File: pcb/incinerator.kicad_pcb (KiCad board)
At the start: 2 copper layers, 51 parts, among them J1 Power Source 12V, J2 IGNITION_MAIN, J3 IGNITION_AFT, J4 VALVE_MAIN, J5 VALVE_AFT_HI, J6 VALVE_AFT_LO, J7 AIRPMP, J8 To Rotary Encoder / Switch, J9 Waveshare 4.2" e-paper, Q1 IRLU120N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

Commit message: First draft of PCB layout
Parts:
- D10: value GRN -> RED
- D11, D9: value GRN -> D; footprint LED_THT:LED_D3.0mm -> Diode_THT:D_DO-41_SOD81_P10.16mm_Horizontal
- D12: value YLW -> RED
- D3, D5: value D -> RED; footprint Diode_THT:D_DO-41_SOD81_P10.16mm_Horizontal -> LED_THT:LED_D3.0mm
- R11, R8: value 15k -> 100
- R12, R9: value 15k -> 1k
- R14, R17: value 100 -> 15k
- R16: value 100 -> 1k
- R3, R6: value 1k -> 15k
- R4: value 1k -> 100
- moved U3 186.9 mm to (91.4, 22.9)
- moved D1 144.8 mm to (38.1, 20.3), turned to 270 degrees
- moved U4 139.9 mm to (129.5, 22.9)
- moved C1 138.2 mm to (40.6, 129.5), turned to 270 degrees
- moved J9 127.9 mm to (154.9, 104.1)
- moved J8 119.5 mm to (109.2, 73.7), turned to 180 degrees
- moved D9 112.1 mm to (38.1, 91.4), turned to 270 degrees
- moved D8 102.4 mm to (58.4, 76.2), turned to 90 degrees
- moved R7 102.1 mm to (48.3, 33.0)
- moved R12 100.4 mm to (53.3, 91.4), turned to 180 degrees
- moved R13 99.7 mm to (61.0, 27.9)
- moved BZ1 97.9 mm to (129.5, 63.5), turned to 180 degrees
- moved D2 94.9 mm to (38.1, 38.1), turned to 270 degrees
- moved R4 94.4 mm to (61.0, 45.7)
- moved D10 94.4 mm to (58.4, 94.0), turned to 90 degrees
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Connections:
- D11 pad 1: Net-(D11-Pad1) -> +12V
- D12 pad 1: Net-(D12-Pad1) -> Net-(D11-Pad2)
- D3 pad 1: +12V -> Net-(D2-Pad2)
- D4 pad 2: Net-(D10-Pad1) -> Net-(D4-Pad2)
- D5 pad 1: +12V -> Net-(D4-Pad2)
- D5 pad 2: Net-(D11-Pad1) -> Net-(D5-Pad2)
- D6 pad 2: Net-(D12-Pad1) -> Net-(D6-Pad2)
- D8 pad 1: Net-(D2-Pad2) -> Net-(D6-Pad2)
- D9 pad 1: Net-(D3-Pad2) -> +12V
- D9 pad 2: Net-(D9-Pad2) -> Net-(D10-Pad1)
- J4 pad 2: Net-(D3-Pad2) -> Net-(D4-Pad2)
- J5 pad 2: Net-(D10-Pad1) -> Net-(D6-Pad2)
- J6 pad 2: Net-(D11-Pad1) -> Net-(D10-Pad1)
- J7 pad 2: Net-(D12-Pad1) -> Net-(D11-Pad2)
- Q3 pad 2: Net-(D3-Pad2) -> Net-(D4-Pad2)
- Q4 pad 2: Net-(D10-Pad1) -> Net-(D6-Pad2)
- Q5 pad 2: Net-(D11-Pad1) -> Net-(D10-Pad1)
- Q6 pad 2: Net-(D12-Pad1) -> Net-(D11-Pad2)
- R11 pad 1: Earth -> Net-(Q4-Pad1)
- R11 pad 2: Net-(Q5-Pad1) -> Net-(R11-Pad2)
- R12 pad 1: Earth -> Net-(D10-Pad2)
- R12 pad 2: Net-(Q6-Pad1) -> +12V
- R14 pad 1: Net-(Q2-Pad1) -> Earth
- R14 pad 2: Net-(R14-Pad2) -> Net-(Q5-Pad1)
- R15 pad 1: Net-(Q3-Pad1) -> Net-(Q5-Pad1)
- R16 pad 1: Net-(Q4-Pad1) -> Net-(D12-Pad2)
- R16 pad 2: Net-(R16-Pad2) -> +12V
- R17 pad 1: Net-(Q5-Pad1) -> Earth
- R17 pad 2: Net-(R17-Pad2) -> Net-(Q6-Pad1)
- R2 pad 1: Net-(D8-Pad2) -> Net-(D3-Pad2)
- R3 pad 1: Net-(D9-Pad2) -> Earth
- R3 pad 2: +12V -> Net-(Q2-Pad1)
- R4 pad 1: Net-(D10-Pad2) -> Net-(Q2-Pad1)
- R4 pad 2: +12V -> Net-(R4-Pad2)
- R5 pad 1: Net-(D11-Pad2) -> Net-(D5-Pad2)
- R6 pad 1: Net-(D12-Pad2) -> Earth
- R6 pad 2: +12V -> Net-(Q3-Pad1)
- R8 pad 1: Earth -> Net-(Q3-Pad1)
- R8 pad 2: Net-(Q2-Pad1) -> Net-(R8-Pad2)
- R9 pad 1: Earth -> Net-(D8-Pad2)
- R9 pad 2: Net-(Q3-Pad1) -> +12V
- U2 pad 10: Net-(R17-Pad2) -> Net-(R15-Pad2)
- U2 pad 7: Net-(R14-Pad2) -> Net-(R4-Pad2)
- U2 pad 8: Net-(R15-Pad2) -> Net-(R8-Pad2)
- U2 pad 9: Net-(R16-Pad2) -> Net-(R11-Pad2)
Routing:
- net Earth: track 0.00 -> 520.4 mm, vias 0 -> 18
- net +12V: track 0.00 -> 259.1 mm, vias 0 -> 7
- net +3V3: track 0.00 -> 177.8 mm, vias 0 -> 2
- net /CLK: track 0.00 -> 152.4 mm, vias 0 -> 4
- net Net-(U2-Pad21): track 0.00 -> 139.7 mm, vias 0 -> 4
- net Net-(U2-Pad25): track 0.00 -> 109.2 mm, vias 0 -> 2
- net Net-(U2-Pad20): track 0.00 -> 106.7 mm, vias 0 -> 2
- net /BUSY: track 0.00 -> 104.1 mm, vias 0 -> 3
- net Net-(R13-Pad2): track 0.00 -> 99.1 mm, vias 0 -> 2
- net Net-(R4-Pad2): track 0.00 -> 86.4 mm, vias 0 -> 2
- net /SW: track 0.00 -> 73.7 mm, vias 0 -> 2
- net Net-(R8-Pad2): track 0.00 -> 73.7 mm, vias 0 -> 2
- net /ROT_CLK: track 0.00 -> 73.7 mm, vias 0 -> 2
- net Net-(U1-Pad3): track 0.00 -> 66.0 mm, vias 0 -> 2
- net /DIN: track 0.00 -> 63.5 mm, vias 0 -> 2
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
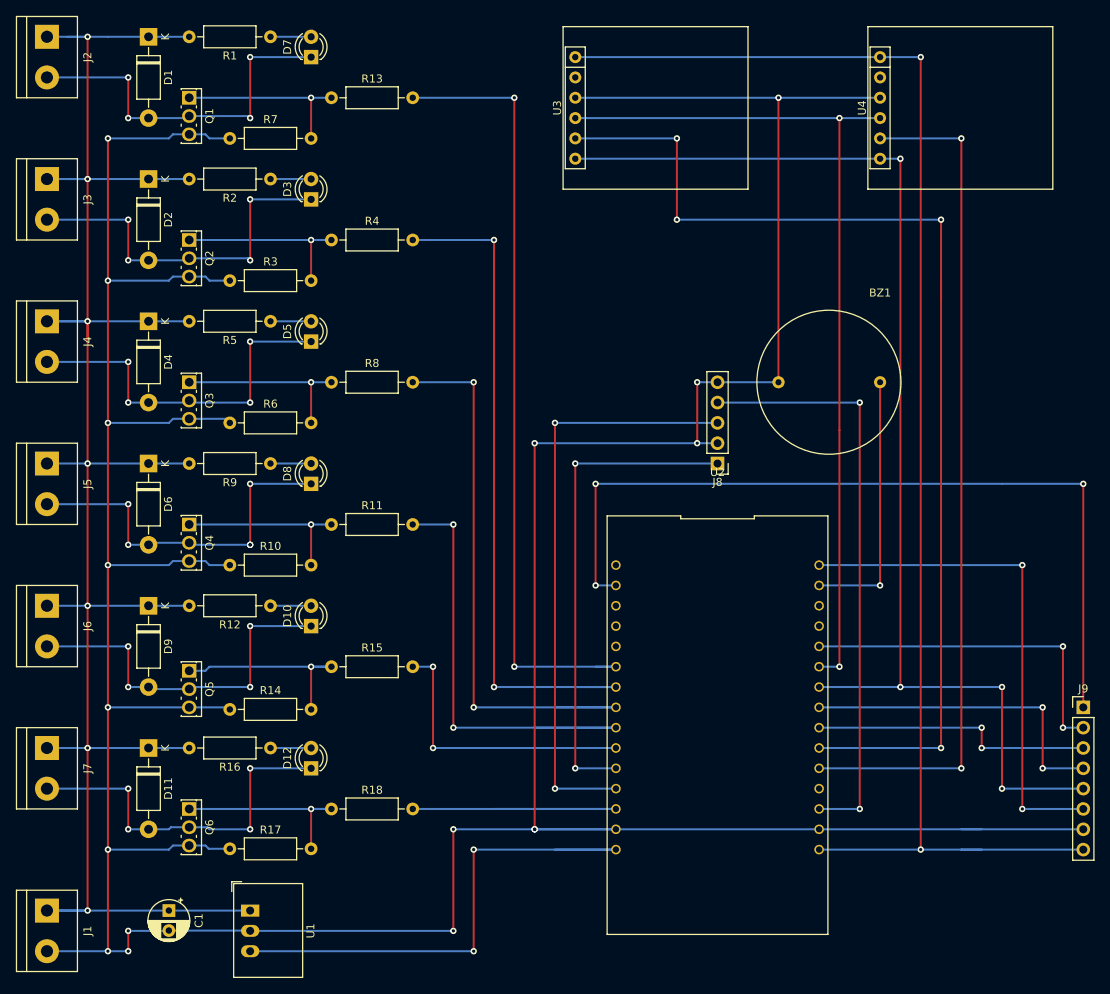
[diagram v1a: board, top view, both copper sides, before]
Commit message: removed breadboard traces from pcb
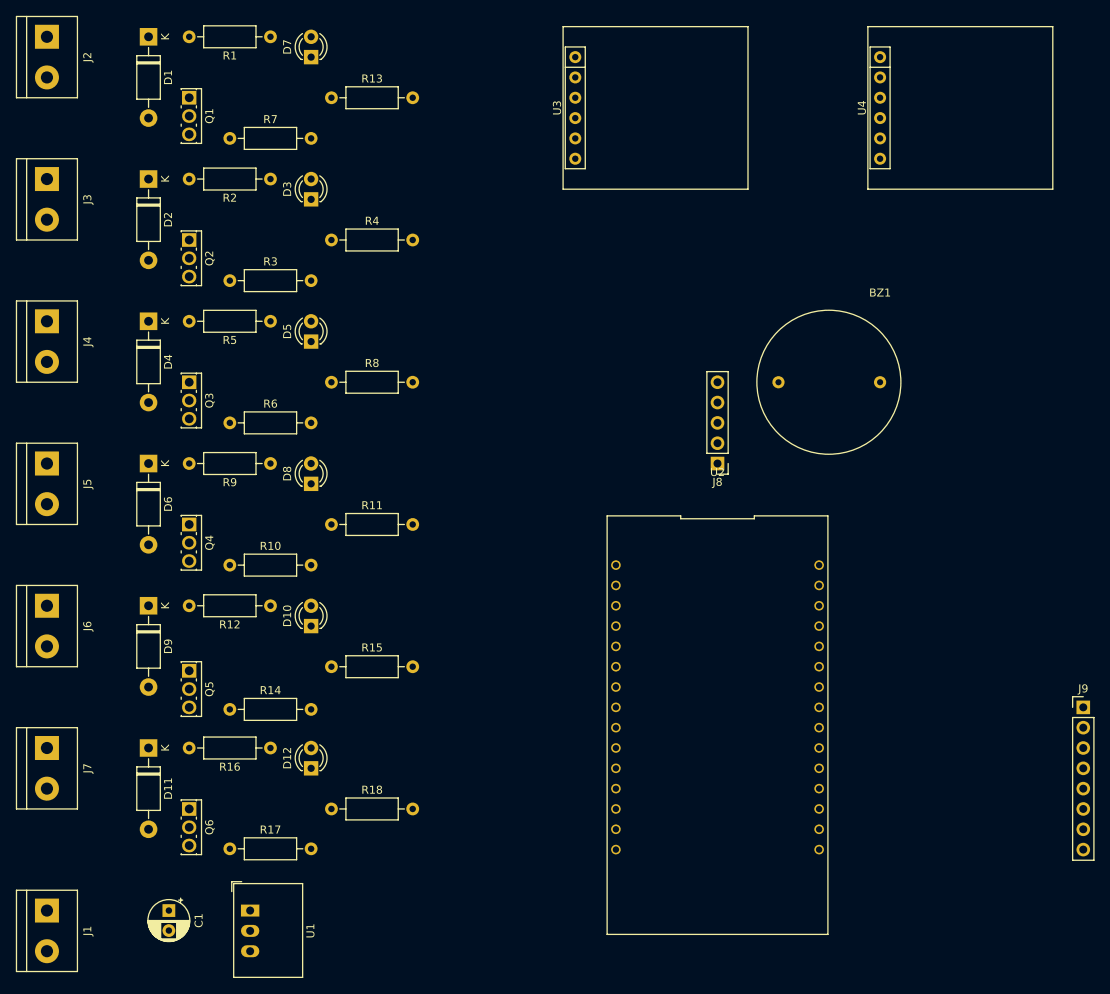
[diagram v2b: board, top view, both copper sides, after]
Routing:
- net Earth: track 520.4 -> 0.00 mm, vias 18 -> 0
- net +12V: track 259.1 -> 0.00 mm, vias 7 -> 0
- net +3V3: track 177.8 -> 0.00 mm, vias 2 -> 0
- net /CLK: track 152.4 -> 0.00 mm, vias 4 -> 0
- net Net-(U2-Pad21): track 139.7 -> 0.00 mm, vias 4 -> 0
- net Net-(U2-Pad25): track 109.2 -> 0.00 mm, vias 2 -> 0
- net Net-(U2-Pad20): track 106.7 -> 0.00 mm, vias 2 -> 0
- net /BUSY: track 104.1 -> 0.00 mm, vias 3 -> 0
- net Net-(R13-Pad2): track 99.1 -> 0.00 mm, vias 2 -> 0
- net Net-(R4-Pad2): track 86.4 -> 0.00 mm, vias 2 -> 0
- net /SW: track 73.7 -> 0.00 mm, vias 2 -> 0
- net Net-(R8-Pad2): track 73.7 -> 0.00 mm, vias 2 -> 0
- net /ROT_CLK: track 73.7 -> 0.00 mm, vias 2 -> 0
- net Net-(U1-Pad3): track 66.0 -> 0.00 mm, vias 2 -> 0
- net /DIN: track 63.5 -> 0.00 mm, vias 2 -> 0
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
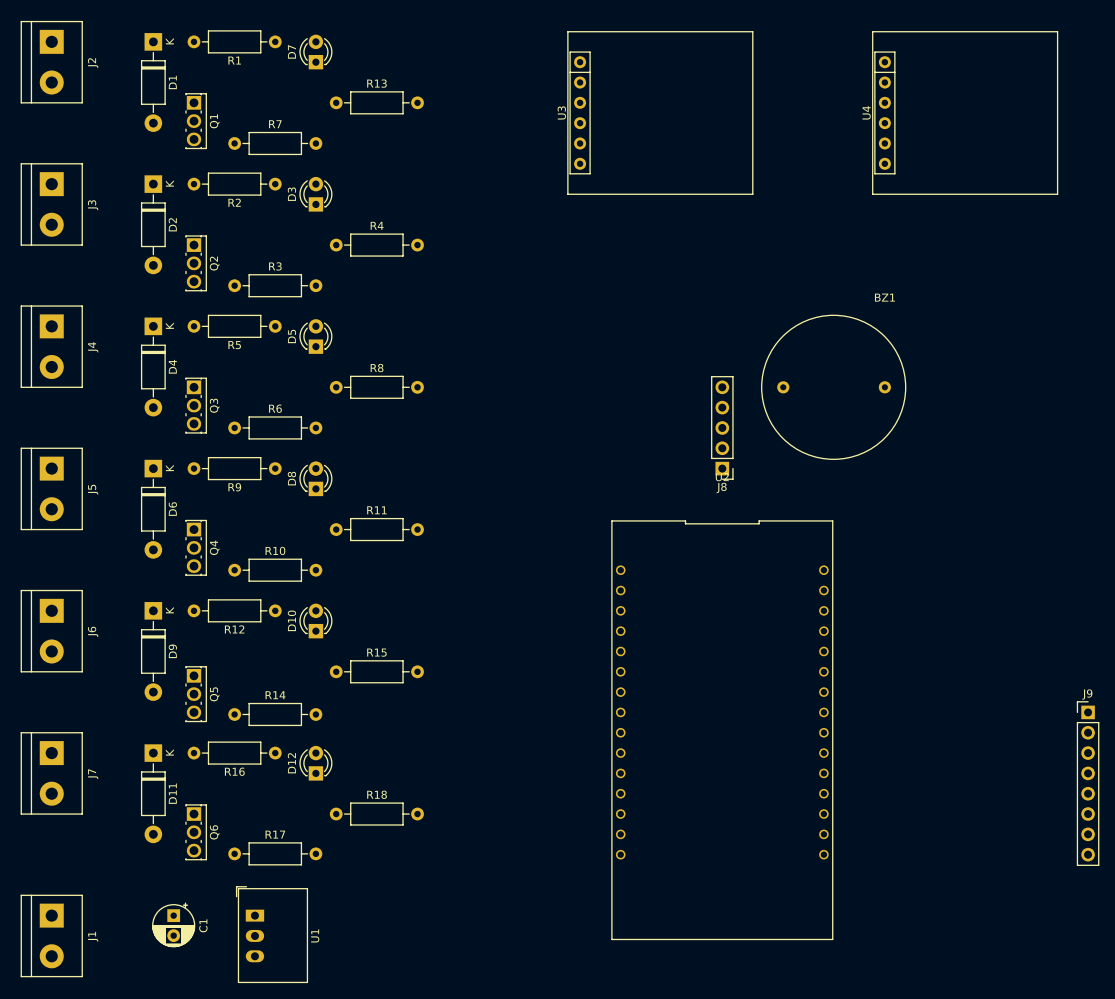
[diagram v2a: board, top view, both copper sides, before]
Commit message: re-worked & shrinked PCB
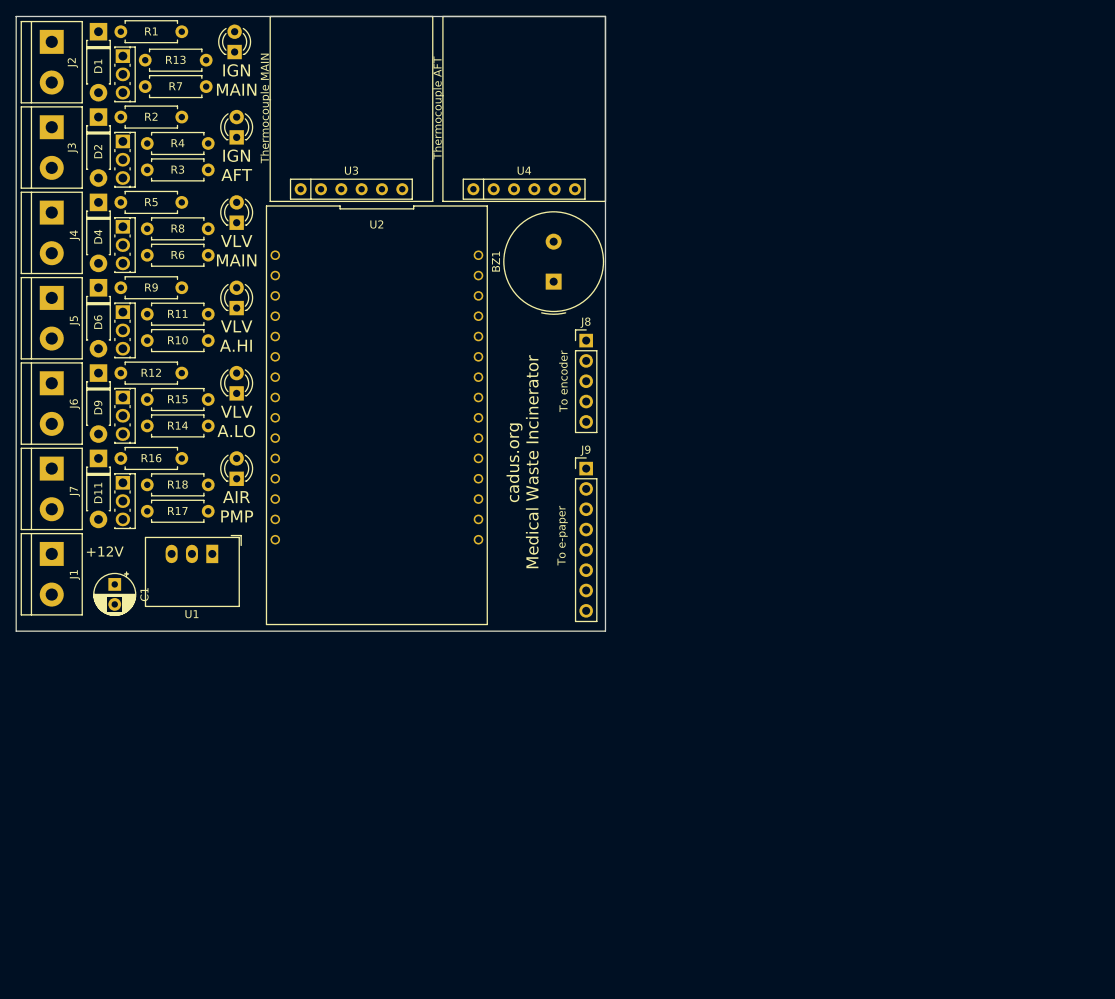
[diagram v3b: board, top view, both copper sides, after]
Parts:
- BZ1: footprint incinerator:Buzzer_BM_15B -> Buzzer_Beeper:Buzzer_TDK_PS1240P02BT_D12.2mm_H6.5mm
- D1, D11, D2, D4, D6, D9: footprint Diode_THT:D_DO-41_SOD81_P10.16mm_Horizontal -> incinerator:D_DO-41_P7.62mm_Custom
- D10, D12, D3, D5, D7, D8: footprint LED_THT:LED_D3.0mm -> incinerator:LED_D3.0mm_Custom
- J8: value To Rotary Encoder / Switch -> To encoder
- J9: value Waveshare 4.2" e-paper -> To e-paper
- Q1, Q2, Q3, Q4, Q5, Q6: footprint Package_TO_SOT_THT:SIPAK_Vertical -> incinerator:SIPAK_Vertical_Custom
- R1, R10, R11, R12, R13, R14, R15, R16, R17, R18, R2, R3, R4, R5, R6, R7, R8, R9: footprint Resistor_THT:R_Axial_DIN0207_L6.3mm_D2.5mm_P10.16mm_Horizontal -> incinerator:R_THT_D2.5mm_P7.62mm_Custom
- U3, U4: value Adafruit_MAX31855 -> Adafruit MAX31855
- moved J9 69.8 mm to (92.2, 73.7)
- moved U2 58.4 mm to (66.0, 64.8)
- moved U4 53.8 mm to (78.1, 38.7), turned to 0 degrees
- moved R18 47.4 mm to (37.3, 75.7)
- moved U1 45.5 mm to (45.5, 84.3), turned to 180 degrees
- moved J1 45.2 mm to (25.4, 84.3)
- moved BZ1 43.5 mm to (88.1, 50.3), turned to 90 degrees
- moved R17 43.0 mm to (45.0, 79.0), turned to 180 degrees
- moved Q6 42.3 mm to (34.3, 75.4)
- moved C1 42.1 mm to (33.3, 88.1)
- moved R15 41.4 mm to (37.3, 65.0)
- moved R16 38.6 mm to (41.7, 72.4)
- moved U3 38.4 mm to (56.5, 38.7), turned to 0 degrees
- moved D12 38.1 mm to (48.5, 74.9)
- moved D11 37.5 mm to (31.2, 72.4)
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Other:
- board outline added: 73.7 x 76.8 mm
- board text added: "+12V"
- board text added: "AIR PMP"
- board text added: "IGN AFT"
- board text added: "IGN MAIN"
- board text added: "Thermocouple AFT"
- board text added: "Thermocouple MAIN"
- board text added: "VLV A.HI"
- board text added: "VLV A.LO"
- board text added: "VLV MAIN"
- board text added: "cadus.org Medical Waste Incinerator"

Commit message: Add PCB infos
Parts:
- moved BZ1 87.1 mm to (168.7, 83.6)
- moved C1 87.1 mm to (113.8, 121.4)
- moved D1 87.1 mm to (111.8, 52.3)
- moved D10 87.1 mm to (129.0, 97.5)
- moved D11 87.1 mm to (111.8, 105.7)
- moved D12 87.1 mm to (129.0, 108.2)
- moved D2 87.1 mm to (111.8, 63.0)
- moved D3 87.1 mm to (129.0, 65.5)
- moved D4 87.1 mm to (111.8, 73.7)
- moved D5 87.1 mm to (129.0, 76.2)
- moved D6 87.1 mm to (111.8, 84.3)
- moved D7 87.1 mm to (128.8, 54.9)
- moved D8 87.1 mm to (129.0, 86.9)
- moved D9 87.1 mm to (111.8, 95.0)
- moved J1 87.1 mm to (105.9, 117.6)
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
